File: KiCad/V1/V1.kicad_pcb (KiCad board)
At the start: 4 copper layers, 98 x 55.2 mm, 83 parts, among them Q1 Q_NMOS_GSD, Q2 Q_NMOS_GSD, T1 Transformer_1P_1S, U1 LMG1210RVRR, U2 OPA2677IDDA, U3 OPA2677IDDA, U4 OPA859QDSGRQ1, U5 OPA859QDSGRQ1, U6 OPA859QDSGRQ1

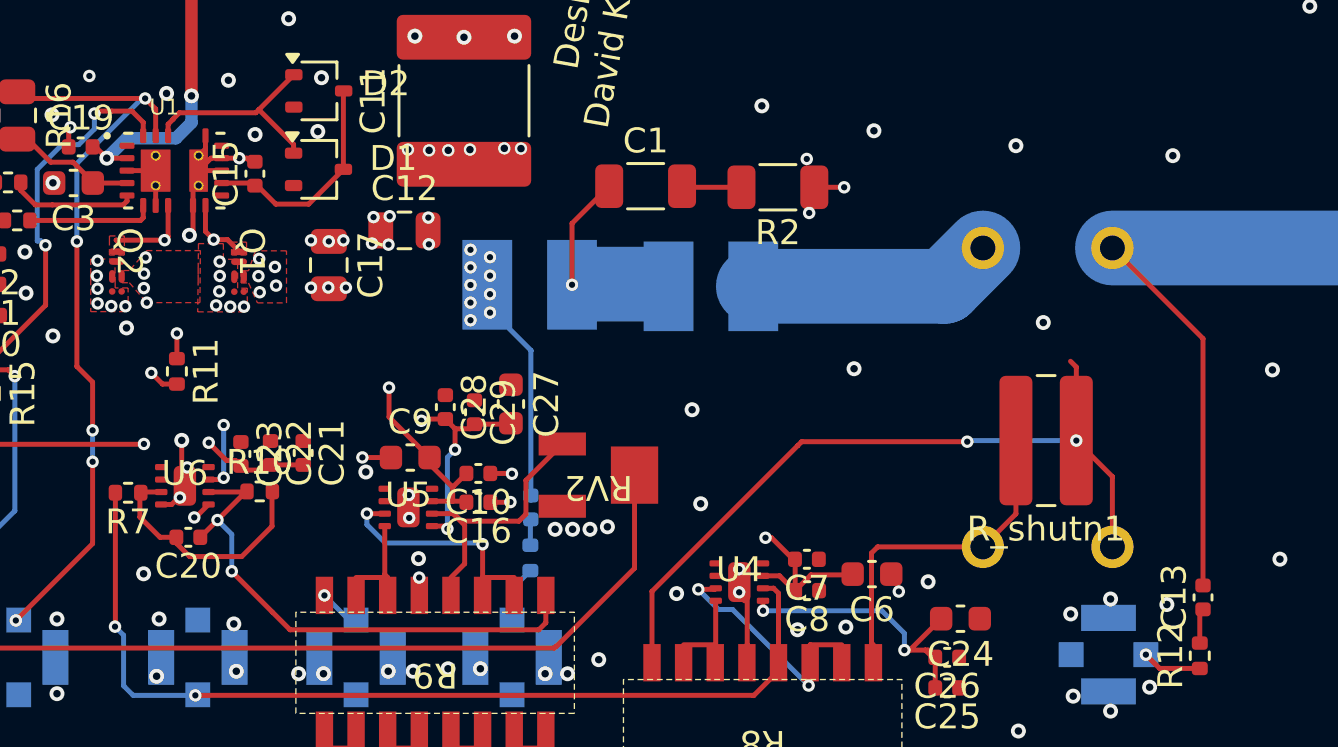
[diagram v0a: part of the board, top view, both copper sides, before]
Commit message: aded alternative path for curent sense signal
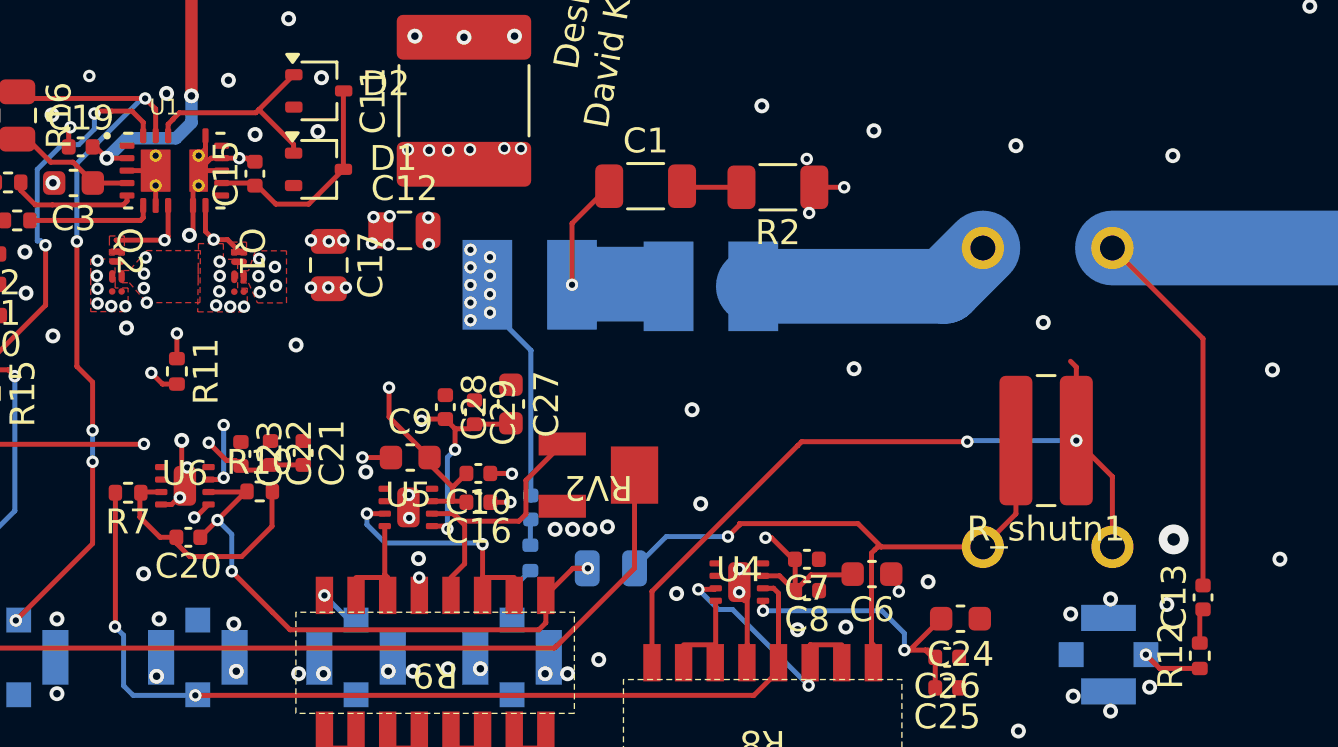
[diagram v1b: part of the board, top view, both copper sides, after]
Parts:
- added R19: 0, Capacitor_SMD:C_0805_2012Metric, B.Cu at (142.2, 58.0)
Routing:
- net Net-(T1-SB): track 13.1 -> 24.2 mm, vias 0 -> 1
- net /V_sens: track 21.3 -> 23.4 mm, vias 2 -> 3
- net GND: vias 155 -> 157
